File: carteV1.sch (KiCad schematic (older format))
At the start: 61 parts, among them CON1 USB-MINI-B, J12 FILTER_IOUT_DUT2, J7 CRYSTAL OUTDUT2, P1 CONN_2X2, P2 CONN_2X2, P3 CONN_2, P4 CONN_2X2, P5 CONN_8, T8 T1-1T, U1 AD9954, U2 LM1117MP-1.8, U3 LM1117MP-1.8, U4 LM1117MP-3.3, U5 MCP2210-SO, X1 25mhz, X2 12mhz

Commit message: Ajout du fichier pour la commande, typon terminé avec plan de masse
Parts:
- added C26: 0,1uF, ~, symbol C
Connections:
- wire segments 192 -> 194
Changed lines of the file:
@@
 Sheet 1 1
 Title "AD9954 - GENERATION SIGNAL HF"
-Date "5 jun 2014"
+Date "13 jun 2014"
 Rev "0.1"
 Comp "Polytech'Tours"
@@
 $EndComp
 $Comp
-L GND #PWR01
-U 1 1 53791D95
-P 3200 7250
-F 0 "#PWR01" H 3200 7250 30  0001 C CNN
-F 1 "GND" H 3200 7180 30  0001 C CNN
-F 2 "" H 3200 7250 60  0000 C CNN
-F 3 "" H 3200 7250 60  0000 C CNN
-	1    3200 7250
-	1    0    0    -1
-$EndComp
-$Comp
 L C C55
 U 1 1 53792166
@@
 Text GLabel 7700 3650 2    60   Input ~ 0
 AVDD
-Text GLabel 7700 3500 2    60   Input ~ 0
+Text GLabel 7950 3500 2    60   Input ~ 0
 GND
 Text GLabel 5100 4700 3    60   Input ~ 0
@@
 Wire Wire Line
 	2500 7100 4450 7100
-Connection ~ 3849 7100
 Connection ~ 4450 7100
 Connection ~ 2500 7100
@@
 	7350 3650 7700 3650
 Wire Wire Line
-	7200 3500 7700 3500
+	7200 3500 7950 3500
 Wire Wire Line
 	5700 4700 5700 4350
@@
 	7200 3300 7250 3300
 Wire Wire Line
-	7650 3300 7650 3500
-Connection ~ 7650 3500
-Wire Wire Line
 	7200 3200 7800 3200
-Wire Wire Line
-	7200 3400 7750 3400
-Wire Wire Line
-	7750 3400 7750 3200
-Connection ~ 7750 3200
 Connection ~ 7650 3300
 Connection ~ 7200 3300
 Connection ~ 7250 3300
 Connection ~ 7200 3200
-Connection ~ 7200 3400
 Wire Wire Line
 	2600 3150 3950 3150
@@
 $EndComp
 Wire Wire Line
-	4000 700  4150 700
-Wire Wire Line
-	4000 1100 4150 1100
+	4000 700  4400 700
+Wire Wire Line
+	4000 1100 4400 1100
 Connection ~ 4150 1100
 Connection ~ 4000 1100
@@
 Connection ~ 2750 750
 Connection ~ 2200 750
+Text GLabel 3200 7250 3    60   Input ~ 0
+GND
+Connection ~ 3200 7250
+Connection ~ 3850 7100
+$Comp
+L C C26
+U 1 1 53917F4C
+P 4400 900
+F 0 "C26" H 4400 1000 40  0000 L CNN
+F 1 "0,1uF" H 4406 815 40  0000 L CNN
+F 2 "~" H 4438 750 30  0000 C CNN
+F 3 "~" H 4400 900 60  0000 C CNN
+	1    4400 900
+	1    0    0    -1
+$EndComp
+Connection ~ 4400 1100
+Connection ~ 4400 700
+Connection ~ 7800 3200
+Connection ~ 7950 3500
+Text GLabel 7550 3400 2    60   Input ~ 0
+AVDD
+Wire Wire Line
+	7200 3400 7550 3400
+Connection ~ 7550 3400
+Connection ~ 7200 3400
+Wire Wire Line
+	7650 3300 7950 3300
+Wire Wire Line
+	7950 3300 7950 3500
+Wire Wire Line
+	5000 1750 5000 1400
+Wire Wire Line
+	5000 1400 5200 1400
+Connection ~ 5000 1750
+Connection ~ 5100 1400
+Connection ~ 5300 1400
+Connection ~ 5000 1400
 $EndSCHEMATC

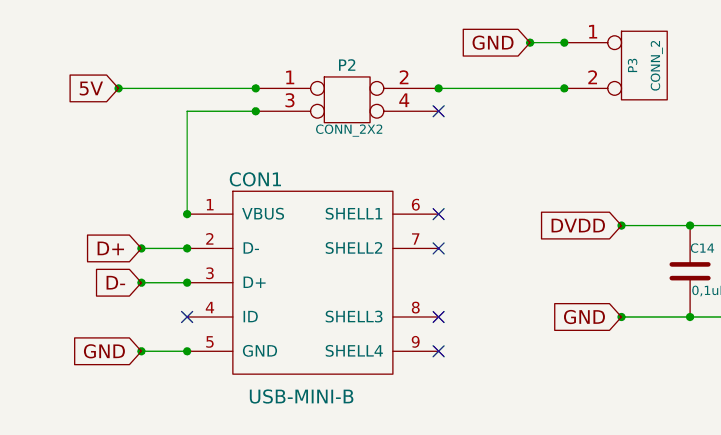
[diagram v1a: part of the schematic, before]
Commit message: Final version without the I/O update pin connected
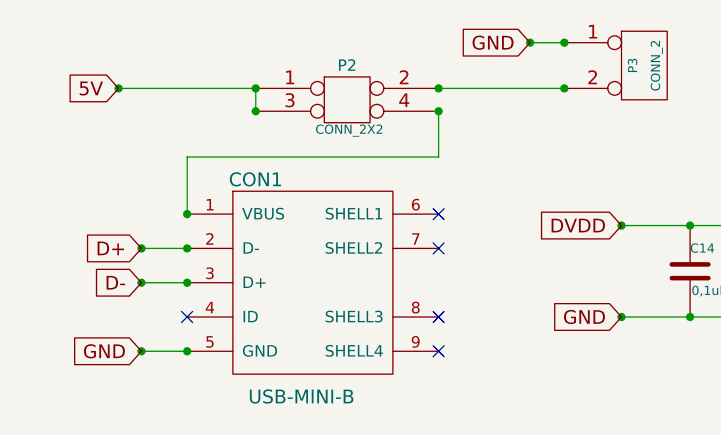
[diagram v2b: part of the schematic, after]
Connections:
- net 5V: now also P2.3
- net at CON1.1 (VBUS): now also P2.4; no longer P2.3
- no-connect marks 19 -> 18
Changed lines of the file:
@@
 Connection ~ 7200 3600
-Wire Wire Line
-	1100 1300 1100 850
-Wire Wire Line
-	1100 850  1400 850
 Wire Wire Line
 	2600 550  2750 550
@@
 Connection ~ 10600 5250
 Connection ~ 2750 550
-Connection ~ 1400 850
 Connection ~ 1400 750
 Connection ~ 8800 2500
@@
 Connection ~ 3050 4950
 Connection ~ 3050 5350
-NoConn ~ 2200 850
 Wire Wire Line
 	2200 750  2750 750
@@
 Connection ~ 5300 1400
 Connection ~ 5000 1400
+Connection ~ 1400 850
+Wire Wire Line
+	1400 750  1400 850
+Wire Wire Line
+	1100 1300 1100 1050
+Wire Wire Line
+	1100 1050 2200 1050
+Wire Wire Line
+	2200 1050 2200 850
+Connection ~ 2200 850
 $EndSCHEMATC

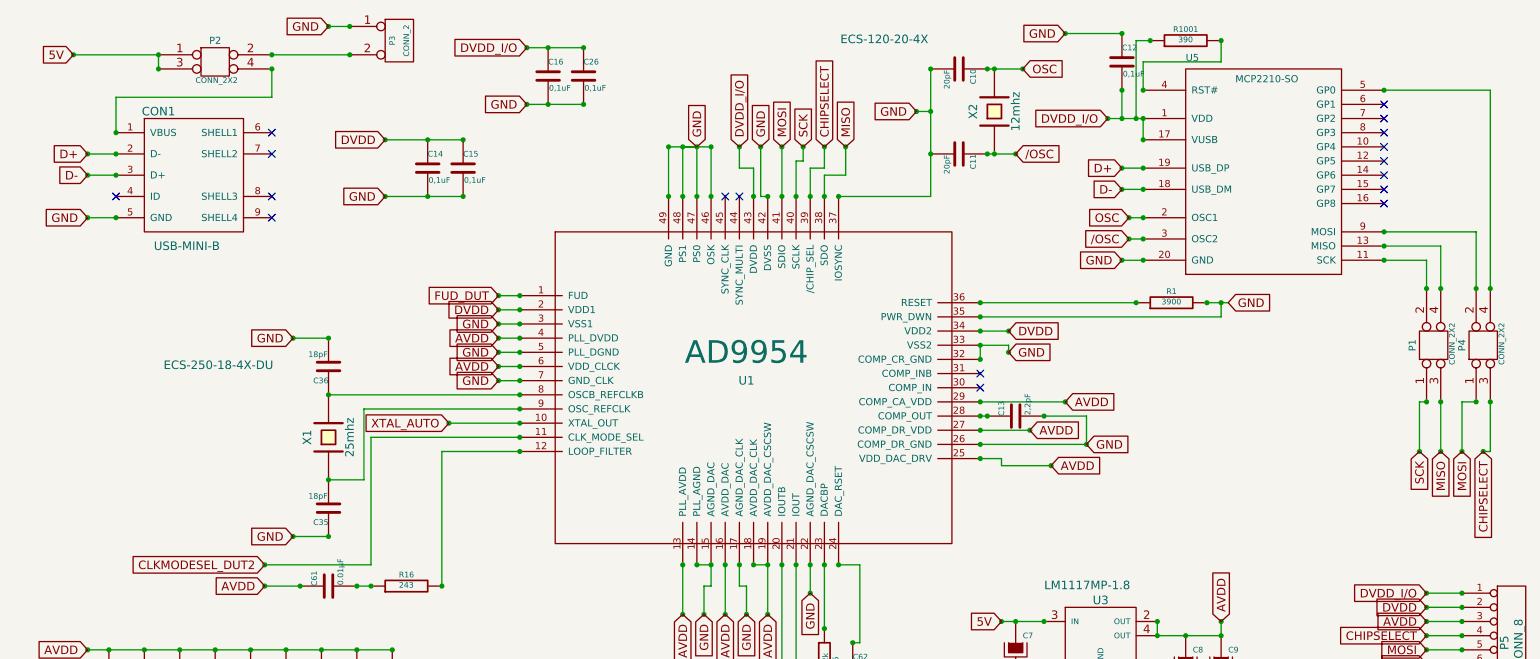
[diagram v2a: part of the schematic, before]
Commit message: Ajout rapport & modification schéma structurel
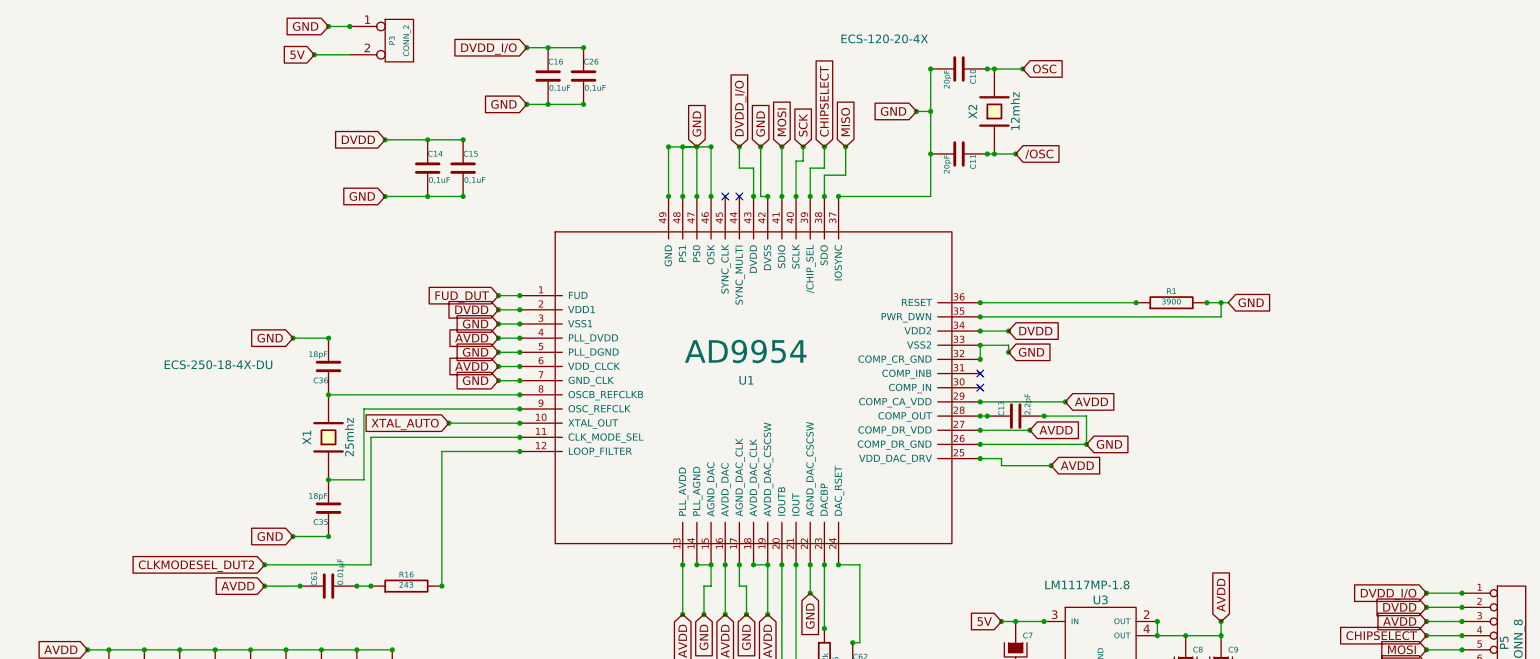
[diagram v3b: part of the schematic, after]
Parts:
- removed C12: 0,1uF, ~, symbol C
- removed CON1: USB-MINI-B, symbol USB-MINI-B
- removed P1, P2, P4: CONN_2X2, symbol CONN_2X2
- removed R1001: 390, ~, symbol R
- removed U5: MCP2210-SO, SSOP-20, symbol MCP2210-SO
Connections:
- net 5V: now also P3.2 (PM)
- no-connect marks 18 -> 5

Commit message: Modification du schéma structurel: - Ajout des 3 alimentations à découpage
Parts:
- removed C1, C2, C3, C4, C5, C6, C7, C8, C9: 10uF, ~, symbol CAPAPOL
- removed C10, C11: 20pF, ~, symbol C
- removed P5: CONN_8, symbol CONN_8
- removed U2, U3: LM1117MP-1.8, symbol LM1117MP-3.3
- removed U4: LM1117MP-3.3, symbol LM1117MP-3.3
- removed X2: 12mhz, ~, symbol CRYSTAL
- added C? (x3): 0.47uF, ~, symbol C
- added C? (x3): 0.1uF, ~, symbol C
- added C? (x3): 680uF, ~, symbol C
- added C? (x3): 100uF, ~, symbol C
- added D? (x3): 1N5820, symbol SS3P4
- added P1: CONN_10, symbol CONN_10
- added R? (x2): 4.7k, ~, symbol R
- added R? (x2): 10k, ~, symbol R
- added R? (x3): 2k, ~, symbol R
- added T? (x3): RL-5530, minicir-KK81, symbol RL-5530
- added U? (x2): LM2588SX-ADJ, ~, symbol LM2588SX-ADJ
- added U?: LM2588SX-3.3, ~, symbol LM2588SX-ADJ
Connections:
- net 5V: now also C?.2, C?.2, C?.2, C?.2, C?.2, C?.2, T?.5 (P1), T?.5 (P1), T?.5 (P1), U?.7 (VIN), U?.7 (VIN), U?.7 (VIN)
- net AVDD: now also C?.1, D?.2 (K), P1.3 (P3); no longer C17.1, C18.1, C19.1, C20.1, C21.1, C22.1, C23.1, C24.1
- net CHIPSELECT: now also P1.4 (P4)
- net DVDD: now also C?.1, D?.2 (K), P1.2 (P2); no longer C14.1
- net MISO: now also P1.6 (P6)
- net MOSI: now also P1.5 (P5)
- net SCK: now also P1.7 (P7)
- net FILTR: now reaches C53.1, C59.1, J12.1 (P), L10.1
- net ADAPT: now reaches C54.2, C55.1, L11.2, T8.4 (P1)
- net DVDD_I/O renamed DGND
- net DGND: now also C15.2, C26.2, R1.2, U1.3 (VSS1), U1.33 (VSS2), U1.35 (PWR_DWN), U1.37 (IOSYNC), U1.42 (DVSS), U1.46 (OSK), U1.47 (PS0), U1.48 (PS1), C?.1, C?.1, C?.1, C?.1, C?.1, C?.2, C?.2, C?.2, C?.2, D?.2 (K), P1.1 (P1), P1.8 (P8), R?.2, T?.1 (S1), T?.1 (S1), U?.1 (ON/OFF), U?.1 (ON/OFF), U?.4 (GND), U?.4 (GND), U?.6 (FSYNC), U?.6 (FSYNC); no longer C16.1
- net FUD_DUT renamed FUD
- net FUD: now also P1.10 (P10)
- net GND renamed AGND
- net AGND: now also C?.1, C?.1, C?.2, C?.2, P1.9 (P9), R?.2, T?.1 (S1), U?.1 (ON/OFF), U?.4 (GND), U?.6 (FSYNC); no longer C14.2, C15.2, C16.2, C17.2, C18.2, C19.2, C20.2, C21.2, C22.2, C23.2, C24.2, C26.2, R1.2, U1.3 (VSS1), U1.33 (VSS2), U1.35 (PWR_DWN), U1.37 (IOSYNC), U1.42 (DVSS), U1.46 (OSK), U1.47 (PS0), U1.48 (PS1)
- new net: R?.1, U?.2 (COMP) (x3)
- new net: R?.1, R?.2, U?.3 (FB) (x2)
- new net: T?.8 (P2), U?.5 (SWITCH) (x3)
- new net: C?.1, R?.2 (x3)
- new net: D?.1 (A), T?.4 (S2) (x3)
- new net: T?.2, T?.3 (ST) (x3)
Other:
- moved on the sheet: C14, C15, C16, C26, C59, C61, P3, R1, R16
